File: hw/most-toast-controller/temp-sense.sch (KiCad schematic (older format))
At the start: 1 part

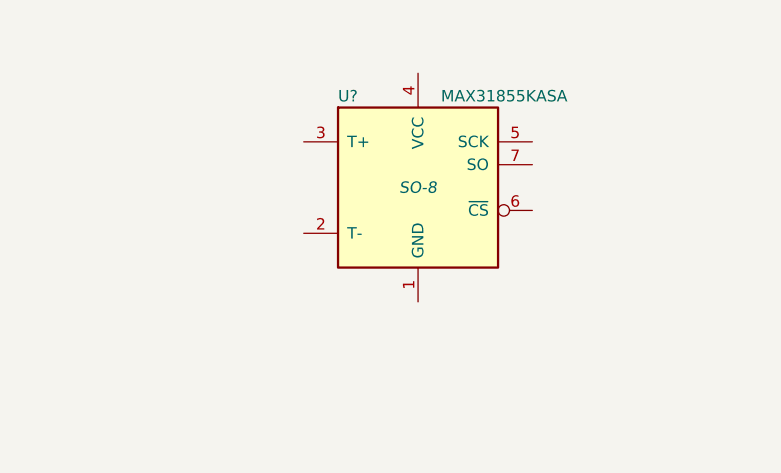
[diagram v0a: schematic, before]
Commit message: most-toast schematic finished.
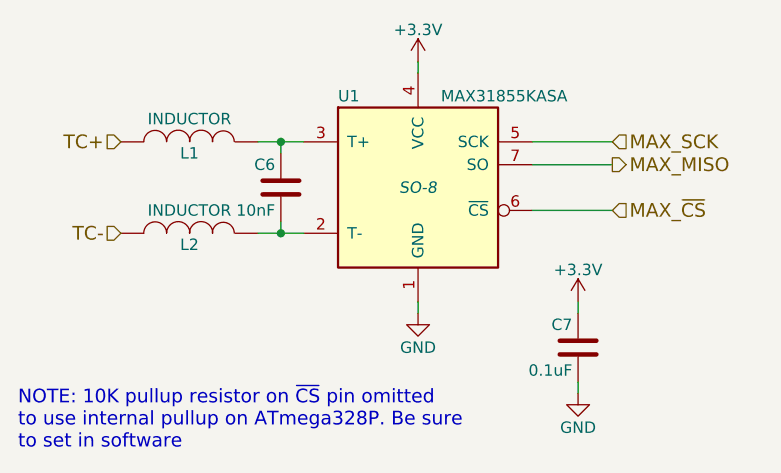
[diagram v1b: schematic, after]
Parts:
- added C6: 10nF, symbol C
- added C7: 0.1uF, symbol C
- added L1, L2: INDUCTOR, symbol INDUCTOR
- gave numbers to parts that had none: 1
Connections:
- net GND: now reaches U1.1 (GND)
- net GND: now also C7.2
- net at U1.2 (T-): now also C6.2, L2.1
- net at U1.3 (T+): now also C6.1, L1.1
- net +3V3: now reaches U1.4 (VCC)
- net +3V3: now also C7.1
- net MAX_SCK: now reaches U1.5 (SCK)
- net MAX_~CS: now reaches U1.6 (~CS~)
- net MAX_MISO: now reaches U1.7 (SO)
- new net TC+: L1.2
- new net TC-: L2.2
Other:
- note added: "NOTE: 10K pullup resistor on ~CS~ pin omitted\nto use internal pullup on ATmega328P. Be sure\nto set in software"
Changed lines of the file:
@@
 LIBS:contrib
 LIBS:valves
+LIBS:most-toast-controller-cache
 EELAYER 25 0
 EELAYER END
 $Descr A4 11693 8268
 encoding utf-8
-Sheet 3 3
+Sheet 3 4
 Title ""
 Date ""
@@
 $EndDescr
 $Comp
-L MAX31855KASA U?
+L MAX31855KASA U1
 U 1 1 56450D43
 P 5350 3300
-F 0 "U?" H 5000 3700 50  0000 L CNN
+F 0 "U1" H 5000 3700 50  0000 L CNN
 F 1 "MAX31855KASA" H 5450 3700 50  0000 L CNN
 F 2 "SO-8" H 5350 3300 50  0000 C CIN
@@
 	1    0    0    -1
 $EndComp
+$Comp
+L INDUCTOR L1
+U 1 1 564BAB3D
+P 4350 3100
+F 0 "L1" V 4300 3100 50  0000 C CNN
+F 1 "INDUCTOR" V 4450 3100 50  0000 C CNN
+F 2 "" H 4350 3100 60  0000 C CNN
+F 3 "" H 4350 3100 60  0000 C CNN
+	1    4350 3100
+	0    1    -1   0
+$EndComp
+$Comp
+L C C6
+U 1 1 564BAB96
+P 4750 3300
+F 0 "C6" H 4775 3400 50  0000 L CNN
+F 1 "10nF" H 4775 3200 50  0000 L CNN
+F 2 "" H 4788 3150 30  0000 C CNN
+F 3 "" H 4750 3300 60  0000 C CNN
+	1    4750 3300
+	-1   0    0    -1
+$EndComp
+$Comp
+L INDUCTOR L2
+U 1 1 564BB062
+P 4350 3500
+F 0 "L2" V 4300 3500 50  0000 C CNN
+F 1 "INDUCTOR" V 4450 3500 50  0000 C CNN
+F 2 "" H 4350 3500 60  0000 C CNN
+F 3 "" H 4350 3500 60  0000 C CNN
+	1    4350 3500
+	0    1    -1   0
+$EndComp
+Wire Wire Line
+	4650 3500 4850 3500
+Wire Wire Line
+	4750 3500 4750 3450
+Connection ~ 4750 3500
+Wire Wire Line
+	4650 3100 4850 3100
+Wire Wire Line
+	4750 3150 4750 3100
+Connection ~ 4750 3100
+Text HLabel 4050 3100 0    60   Input ~ 0
+TC+
+Text HLabel 4050 3500 0    60   Input ~ 0
+TC-
+$Comp
+L C C7
+U 1 1 564BB456
+P 6050 4000
+F 0 "C7" H 6075 4100 50  0000 L CNN
+F 1 "0.1uF" H 6075 3900 50  0000 L CNN
+F 2 "" H 6088 3850 30  0000 C CNN
+F 3 "" H 6050 4000 60  0000 C CNN
+	1    6050 4000
+	-1   0    0    -1
+$EndComp
+$Comp
+L +3.3V #PWR14
+U 1 1 564BB5C4
+P 5350 2750
+F 0 "#PWR14" H 5350 2600 50  0001 C CNN
+F 1 "+3.3V" H 5350 2890 50  0000 C CNN
+F 2 "" H 5350 2750 60  0000 C CNN
+F 3 "" H 5350 2750 60  0000 C CNN
+	1    5350 2750
+	1    0    0    -1
+$EndComp
+Wire Wire Line
+	5850 3400 6200 3400
+$Comp
+L GND #PWR16
+U 1 1 564BB67E
+P 5350 3850
+F 0 "#PWR16" H 5350 3600 50  0001 C CNN
+F 1 "GND" H 5350 3700 50  0000 C CNN
+F 2 "" H 5350 3850 60  0000 C CNN
+F 3 "" H 5350 3850 60  0000 C CNN
+	1    5350 3850
+	1    0    0    -1
+$EndComp
+Wire Wire Line
+	5350 3800 5350 3850
+Wire Wire Line
+	5350 2750 5350 2800
+$Comp
+L +3.3V #PWR15
+U 1 1 564BBA4F
+P 6050 3800
+F 0 "#PWR15" H 6050 3650 50  0001 C CNN
+F 1 "+3.3V" H 6050 3940 50  0000 C CNN
+F 2 "" H 6050 3800 60  0000 C CNN
+F 3 "" H 6050 3800 60  0000 C CNN
+	1    6050 3800
+	1    0    0    -1
+$EndComp
+$Comp
+L GND #PWR17
+U 1 1 564BBA6C
+P 6050 4200
+F 0 "#PWR17" H 6050 3950 50  0001 C CNN
+F 1 "GND" H 6050 4050 50  0000 C CNN
+F 2 "" H 6050 4200 60  0000 C CNN
+F 3 "" H 6050 4200 60  0000 C CNN
+	1    6050 4200
+	1    0    0    -1
+$EndComp
+Wire Wire Line
+	6050 4200 6050 4150
+Wire Wire Line
+	6050 3800 6050 3850
+Wire Wire Line
+	5850 3100 6200 3100
+Wire Wire Line
+	5850 3200 6200 3200
+Text HLabel 6200 3100 2    60   Input ~ 0
+MAX_SCK
+Text HLabel 6200 3200 2    60   Output ~ 0
+MAX_MISO
+Text HLabel 6200 3400 2    60   Input ~ 0
+MAX_~CS
+Text Notes 3600 4450 0    60   ~ 0
+NOTE: 10K pullup resistor on ~CS~ pin omitted\nto use internal pullup on ATmega328P. Be sure\nto set in software
 $EndSCHEMATC

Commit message: started putting most-toast on a board. Turns out one inch makes for very very small PCB
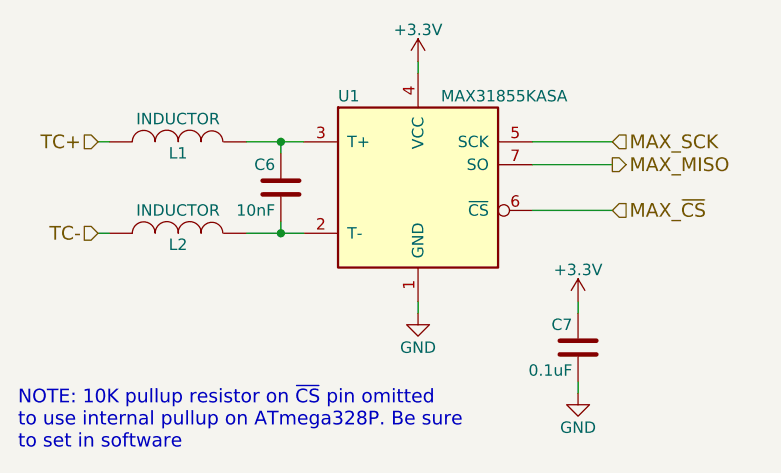
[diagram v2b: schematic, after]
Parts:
- C6, C7, L1, L2: footprint (none) -> Capacitors_SMD:C_0805_HandSoldering
- U1: footprint SO-8 -> Housings_SOIC:SOIC-8_3.9x4.9mm_Pitch1.27mm
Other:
- moved on the sheet: L1, L2
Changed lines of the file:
@@
 EESchema Schematic File Version 2
+LIBS:regul
 LIBS:power
 LIBS:device
@@
 LIBS:conn
 LIBS:linear
-LIBS:regul
 LIBS:74xx
 LIBS:cmos4000
@@
 F 0 "U1" H 5000 3700 50  0000 L CNN
 F 1 "MAX31855KASA" H 5450 3700 50  0000 L CNN
-F 2 "SO-8" H 5350 3300 50  0000 C CIN
+F 2 "Housings_SOIC:SOIC-8_3.9x4.9mm_Pitch1.27mm" H 5350 3300 50  0001 C CIN
 F 3 "" H 5350 3300 60  0000 C CNN
 	1    5350 3300
@@
 L INDUCTOR L1
 U 1 1 564BAB3D
-P 4350 3100
-F 0 "L1" V 4300 3100 50  0000 C CNN
-F 1 "INDUCTOR" V 4450 3100 50  0000 C CNN
-F 2 "" H 4350 3100 60  0000 C CNN
-F 3 "" H 4350 3100 60  0000 C CNN
-	1    4350 3100
+P 4300 3100
+F 0 "L1" V 4250 3100 50  0000 C CNN
+F 1 "INDUCTOR" V 4400 3100 50  0000 C CNN
+F 2 "Capacitors_SMD:C_0805_HandSoldering" H 4300 3100 60  0001 C CNN
+F 3 "" H 4300 3100 60  0000 C CNN
+	1    4300 3100
 	0    1    -1   0
 $EndComp
@@
 F 0 "C6" H 4775 3400 50  0000 L CNN
 F 1 "10nF" H 4775 3200 50  0000 L CNN
-F 2 "" H 4788 3150 30  0000 C CNN
+F 2 "Capacitors_SMD:C_0805_HandSoldering" H 4788 3150 30  0001 C CNN
 F 3 "" H 4750 3300 60  0000 C CNN
 	1    4750 3300
@@
 L INDUCTOR L2
 U 1 1 564BB062
-P 4350 3500
-F 0 "L2" V 4300 3500 50  0000 C CNN
-F 1 "INDUCTOR" V 4450 3500 50  0000 C CNN
-F 2 "" H 4350 3500 60  0000 C CNN
-F 3 "" H 4350 3500 60  0000 C CNN
-	1    4350 3500
+P 4300 3500
+F 0 "L2" V 4250 3500 50  0000 C CNN
+F 1 "INDUCTOR" V 4400 3500 50  0000 C CNN
+F 2 "Capacitors_SMD:C_0805_HandSoldering" H 4300 3500 60  0001 C CNN
+F 3 "" H 4300 3500 60  0000 C CNN
+	1    4300 3500
 	0    1    -1   0
 $EndComp
 Wire Wire Line
-	4650 3500 4850 3500
+	4600 3500 4850 3500
 Wire Wire Line
 	4750 3500 4750 3450
 Connection ~ 4750 3500
 Wire Wire Line
-	4650 3100 4850 3100
+	4600 3100 4850 3100
 Wire Wire Line
 	4750 3150 4750 3100
 Connection ~ 4750 3100
-Text HLabel 4050 3100 0    60   Input ~ 0
+Text HLabel 3950 3100 0    60   Input ~ 0
 TC+
-Text HLabel 4050 3500 0    60   Input ~ 0
+Text HLabel 3950 3500 0    60   Input ~ 0
 TC-
 $Comp
@@
 F 0 "C7" H 6075 4100 50  0000 L CNN
 F 1 "0.1uF" H 6075 3900 50  0000 L CNN
-F 2 "" H 6088 3850 30  0000 C CNN
+F 2 "Capacitors_SMD:C_0805_HandSoldering" H 6088 3850 30  0001 C CNN
 F 3 "" H 6050 4000 60  0000 C CNN
 	1    6050 4000
@@
 $EndComp
 $Comp
-L +3.3V #PWR14
+L +3.3V #PWR014
 U 1 1 564BB5C4
 P 5350 2750
-F 0 "#PWR14" H 5350 2600 50  0001 C CNN
+F 0 "#PWR014" H 5350 2600 50  0001 C CNN
 F 1 "+3.3V" H 5350 2890 50  0000 C CNN
 F 2 "" H 5350 2750 60  0000 C CNN
@@
 	5850 3400 6200 3400
 $Comp
-L GND #PWR16
+L GND #PWR015
 U 1 1 564BB67E
 P 5350 3850
-F 0 "#PWR16" H 5350 3600 50  0001 C CNN
+F 0 "#PWR015" H 5350 3600 50  0001 C CNN
 F 1 "GND" H 5350 3700 50  0000 C CNN
 F 2 "" H 5350 3850 60  0000 C CNN
@@
 	5350 2750 5350 2800
 $Comp
-L +3.3V #PWR15
+L +3.3V #PWR016
 U 1 1 564BBA4F
 P 6050 3800
-F 0 "#PWR15" H 6050 3650 50  0001 C CNN
+F 0 "#PWR016" H 6050 3650 50  0001 C CNN
 F 1 "+3.3V" H 6050 3940 50  0000 C CNN
 F 2 "" H 6050 3800 60  0000 C CNN
@@
 $EndComp
 $Comp
-L GND #PWR17
+L GND #PWR017
 U 1 1 564BBA6C
 P 6050 4200
-F 0 "#PWR17" H 6050 3950 50  0001 C CNN
+F 0 "#PWR017" H 6050 3950 50  0001 C CNN
 F 1 "GND" H 6050 4050 50  0000 C CNN
 F 2 "" H 6050 4200 60  0000 C CNN
@@
 Text Notes 3600 4450 0    60   ~ 0
 NOTE: 10K pullup resistor on ~CS~ pin omitted\nto use internal pullup on ATmega328P. Be sure\nto set in software
+Wire Wire Line
+	4000 3500 3950 3500
+Wire Wire Line
+	4000 3100 3950 3100
 $EndSCHEMATC
